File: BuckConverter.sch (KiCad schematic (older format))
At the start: 8 parts, among them IC1 XL1509-ADJE1

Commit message: First layouting
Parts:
- IC1: footprint SOIC127P600X175-8N -> CSE:SOIC127P600X175-8N; symbol CSE:XL1509-ADJE1 -> ESP32_Tasmota_Fan-rescue:XL1509-ADJE1-CSE
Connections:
- net labels added: OUTPUT, VIN, VOUT
- net labels removed: +12V, +3V3
- wire segments 36 -> 34
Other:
- note added: "Feedback Pin (FB). Through an external resistor divider\nnetwork, Feedback senses the output voltage and regulates it.\nThe feedback threshold voltage is 1.23V\nSelect R1 to be approximately 1K, use a 1% resistor for best stability\n\nVOUT = 1.23 * (1+R2/R1)"
- note removed: "Feedback Pin (FB). Through an external resistor divider\nnetwork, Feedback senses the output voltage and regulates it.\nThe feedback threshold voltage is 1.23V\nSelect R1 to be approximately 1K, use a 1% resistor for best stability"
- note removed: "VOUT = 1.23 * (1+R2/R1)"
- moved on the sheet: C2, C3, C4, D2, L1, R20, R21

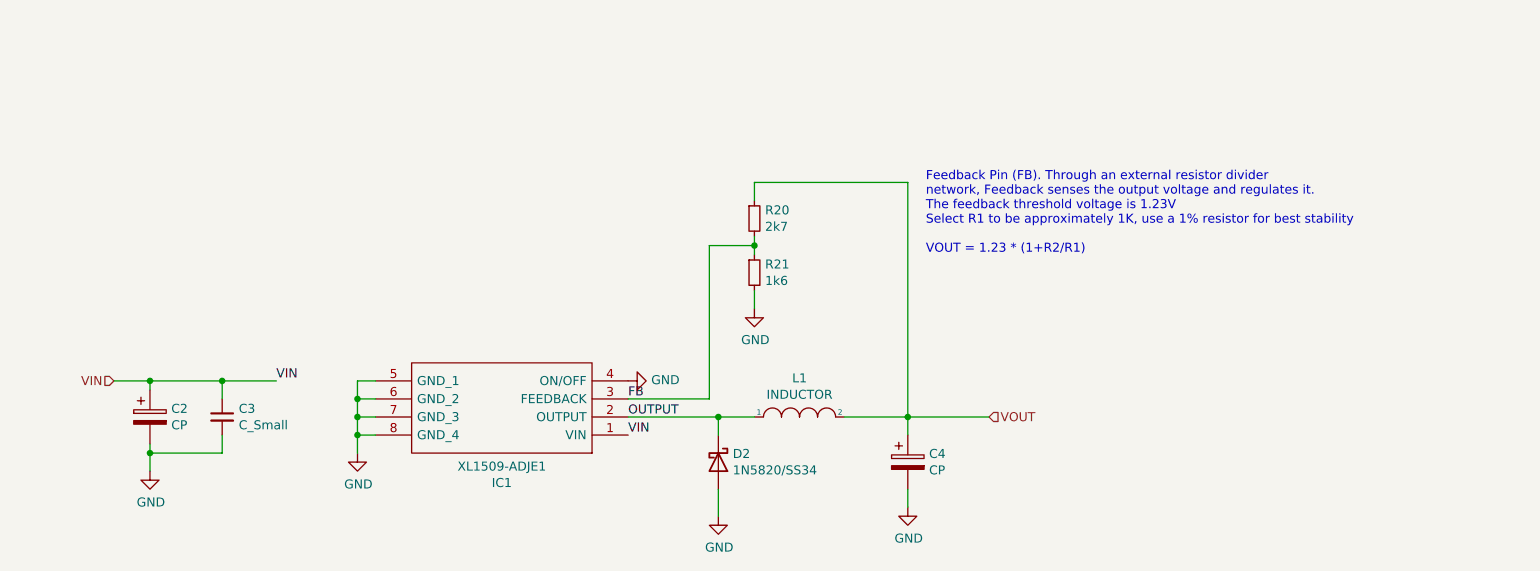
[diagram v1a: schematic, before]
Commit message: First iteration with new ES32 - but not S2
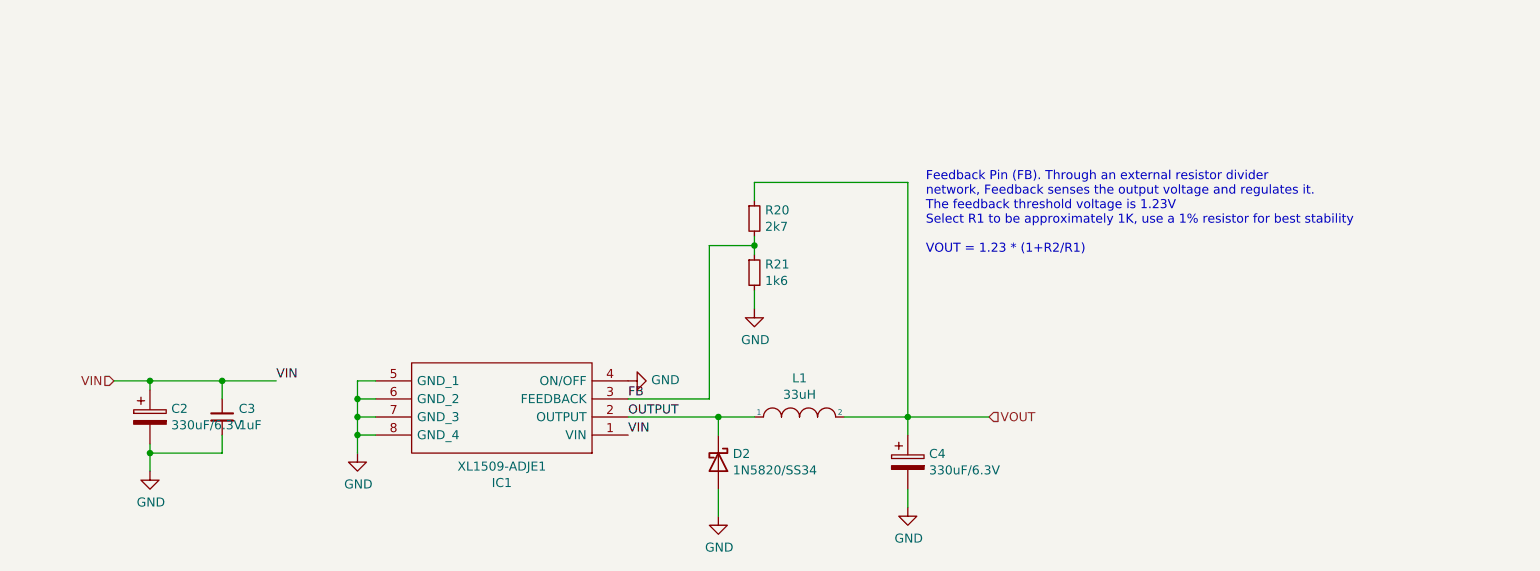
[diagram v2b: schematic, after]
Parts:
- C2, C4: value CP -> 330uF/6.3V; footprint Capacitor_Tantalum_SMD:CP_EIA-7343-30_AVX-N -> Capacitor_Tantalum_SMD:CP_EIA-3528-15_AVX-H; LCSC (none) -> C16133
- C3: value C_Small -> 1uF; LCSC (none) -> C1779
- D2: LCSC (none) -> C8678
- IC1: LCSC (none) -> C74192
- L1: value INDUCTOR -> 33uH; footprint Inductor_SMD:L_10.4x10.4_H4.8 -> Inductor_SMD:L_TDK_SLF7045; LCSC (none) -> C13754
- R20: LCSC (none) -> C17530
- R21: LCSC (none) -> C17394
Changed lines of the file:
@@
 $Descr A4 11693 8268
 encoding utf-8
-Sheet 7 7
-Title ""
+Sheet 4 7
+Title "DC/DC Converter 12V->3.3V"
 Date ""
 Rev ""
@@
 F 10 "" H 6450 3250 50  0001 L CNN "Arrow Part Number"
 F 11 "" H 6450 3150 50  0001 L CNN "Arrow Price/Stock"
+F 12 "C74192" H 5200 3950 50  0001 C CNN "LCSC"
 	1    5200 3950
 	-1   0    0    1
@@
 P 2950 3850
 F 0 "C3" H 3042 3896 50  0000 L CNN
-F 1 "C_Small" H 3042 3805 50  0000 L CNN
+F 1 "1uF" H 3042 3805 50  0000 L CNN
 F 2 "Capacitor_SMD:C_0805_2012Metric" H 2950 3850 50  0001 C CNN
 F 3 "~" H 2950 3850 50  0001 C CNN
+F 4 "C1779" H 2950 3850 50  0001 C CNN "LCSC"
 	1    2950 3850
 	1    0    0    -1
@@
 P 2550 3850
 F 0 "C2" H 2668 3896 50  0000 L CNN
-F 1 "CP" H 2668 3805 50  0000 L CNN
-F 2 "Capacitor_Tantalum_SMD:CP_EIA-7343-30_AVX-N" H 2588 3700 50  0001 C CNN
+F 1 "330uF/6.3V" H 2668 3805 50  0000 L CNN
+F 2 "Capacitor_Tantalum_SMD:CP_EIA-3528-15_AVX-H" H 2588 3700 50  0001 C CNN
 F 3 "~" H 2550 3850 50  0001 C CNN
+F 4 "C16133" H 2550 3850 50  0001 C CNN "LCSC"
 	1    2550 3850
 	1    0    0    -1
@@
 P 6150 3850
 F 0 "L1" H 6150 4065 50  0000 C CNN
-F 1 "INDUCTOR" H 6150 3974 50  0000 C CNN
-F 2 "Inductor_SMD:L_10.4x10.4_H4.8" H 6150 3850 50  0001 C CNN
+F 1 "33uH" H 6150 3974 50  0000 C CNN
+F 2 "Inductor_SMD:L_TDK_SLF7045" H 6150 3850 50  0001 C CNN
 F 3 "~" H 6150 3850 50  0001 C CNN
+F 4 "C13754" H 6150 3850 50  0001 C CNN "LCSC"
 	1    6150 3850
 	1    0    0    -1
@@
 P 6750 4100
 F 0 "C4" H 6868 4146 50  0000 L CNN
-F 1 "CP" H 6868 4055 50  0000 L CNN
-F 2 "Capacitor_Tantalum_SMD:CP_EIA-7343-30_AVX-N" H 6788 3950 50  0001 C CNN
+F 1 "330uF/6.3V" H 6868 4055 50  0000 L CNN
+F 2 "Capacitor_Tantalum_SMD:CP_EIA-3528-15_AVX-H" H 6788 3950 50  0001 C CNN
 F 3 "~" H 6750 4100 50  0001 C CNN
+F 4 "C16133" H 6750 4100 50  0001 C CNN "LCSC"
 	1    6750 4100
 	1    0    0    -1
@@
 F 2 "Diode_SMD:D_SMA" H 5700 4100 50  0001 C CNN
 F 3 "~" H 5700 4100 50  0001 C CNN
+F 4 "C8678" H 5700 4100 50  0001 C CNN "LCSC"
 	1    5700 4100
 	0    1    1    0
@@
 F 2 "Resistor_SMD:R_0805_2012Metric" H 5900 2750 50  0001 C CNN
 F 3 "~" H 5900 2750 50  0001 C CNN
+F 4 "C17530" H 5900 2750 50  0001 C CNN "LCSC"
 	1    5900 2750
 	1    0    0    -1
@@
 F 2 "Resistor_SMD:R_0805_2012Metric" H 5900 3050 50  0001 C CNN
 F 3 "~" H 5900 3050 50  0001 C CNN
+F 4 "C17394" H 5900 3050 50  0001 C CNN "LCSC"
 	1    5900 3050
 	1    0    0    -1
